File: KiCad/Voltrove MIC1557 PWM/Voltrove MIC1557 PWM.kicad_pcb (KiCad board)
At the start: 2 copper layers, 70 x 20 mm, 32 parts, among them IC1 DS1809Z-010+, IC2 NCV4264-2ST50T3G, J1 BAT-, J2 510-, J3 VIN+, J4 PAD_Fire2, J5 PAD_Fire1, J6 VM-, J7 VM+, Q1 SSM3J334R_LF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

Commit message: v2
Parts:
- moved J7 1.66 mm to (128.0, 105.0)
- moved J6 1.50 mm to (125.0, 105.0)
- moved R4 1.00 mm to (175.4, 107.4)
- moved R1 0.50 mm to (168.4, 107.4)
- moved R3 0.50 mm to (173.1, 107.4)
- turned Q1 to 270 degrees
- turned R5 to 0 degrees
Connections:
- net Net-(C3-Pad1) renamed /5V+toC3
- net Net-(C4-Pad1) renamed /D2toSTR
- net Net-(D1-Pad1) renamed /POT0%
- net Net-(D1-Pad3) renamed /POT100%
- net Net-(D3-Pad1) renamed /VIN+toFire1
- net Net-(D3-Pad2) renamed /R5toD3
- net Net-(IC1-Pad6) renamed /POTWIPER
- net Net-(R2-Pad2) renamed /U1toR2
- net Net-(R3-Pad1) renamed /U1OUT
- net Net-(R5-Pad2) renamed /VIN+toR5
- C2 pad 1: /VIN+ -> /VIN+fromQ1Source
- IC2 pad 1: /VIN+ -> /VIN+fromQ1Source
- J3 pad 1: /VIN+ -> /VIN+toSwitch
- J4 pad 1: /VIN+ -> /VIN+toQ1Drain
- J7 pad 1: /VIN+ -> /VIN+fromQ1Source
- Q1 pad 2: /VIN+ -> /VIN+fromQ1Source
- Q1 pad 3: /VIN+ -> /VIN+toQ1Drain
- R2 pad 1: /VIN+ -> /VIN+fromQ1Source
- S1 pad 3: /VIN+ -> /VIN+toQ1Drain
- S1 pad 4: /VIN+ -> /VIN+toQ1Drain
- S4 pad 1: /VIN+ -> /VIN+toSwitch
- U1 pad 4: /VIN+ -> /VIN+fromQ1Source
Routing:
- net /VIN+: track 160.5 -> 0.00 mm, vias 2 -> 0
- net /VIN+fromQ1Source: track 0.00 -> 97.0 mm, vias 0 -> 3
- net /VIN+toQ1Drain: track 0.00 -> 86.1 mm, vias 0 -> 1
- net /POTWIPER: track 22.9 -> 39.9 mm
- net /5V+toC3: track 42.8 -> 30.6 mm, vias 2 -> 3
- net Net-(C1-Pad1): track 37.8 -> 25.8 mm
- net /VIN+toFire1: track 74.8 -> 84.5 mm, vias 1 -> 0
- net Net-(Q2-Pad4): track 33.7 -> 27.4 mm
- net /VIN+toSwitch: track 0.00 -> 5.62 mm
- net GND: track 135.5 -> 129.9 mm, vias 3 -> 1
- net /VIN+toR5: track 9.18 -> 5.73 mm
- net /UP: track 18.2 -> 20.7 mm
- net /D2toSTR: track 35.3 -> 37.7 mm
- net /R5toD3: track 5.01 -> 3.72 mm

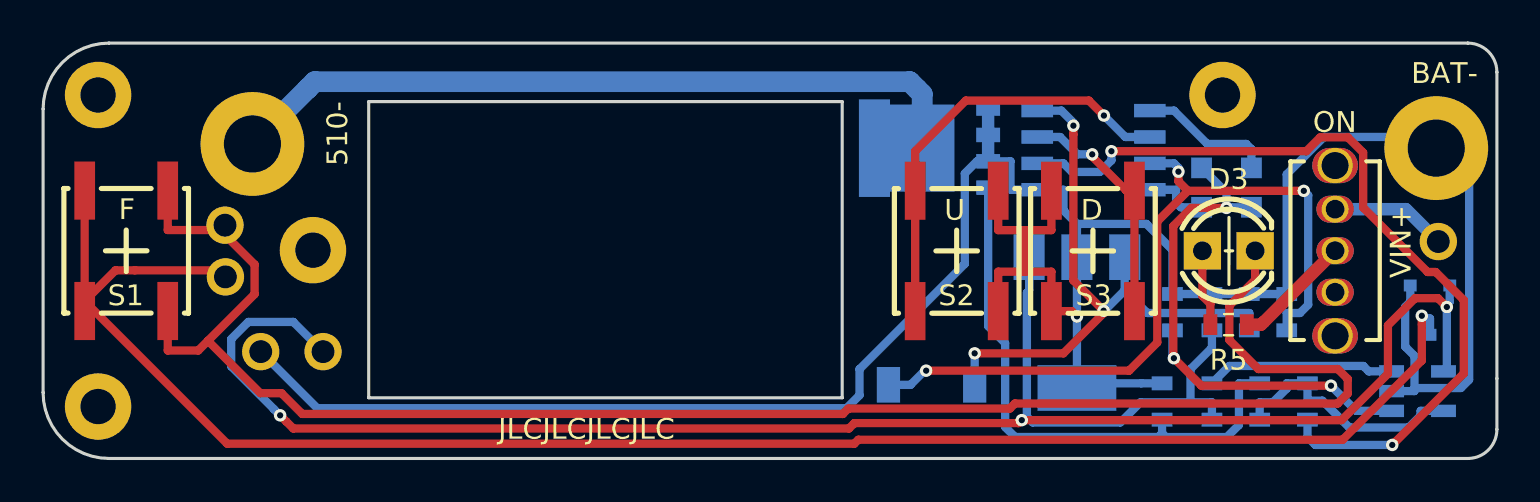
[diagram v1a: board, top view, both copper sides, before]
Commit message: v3 suggestions from David
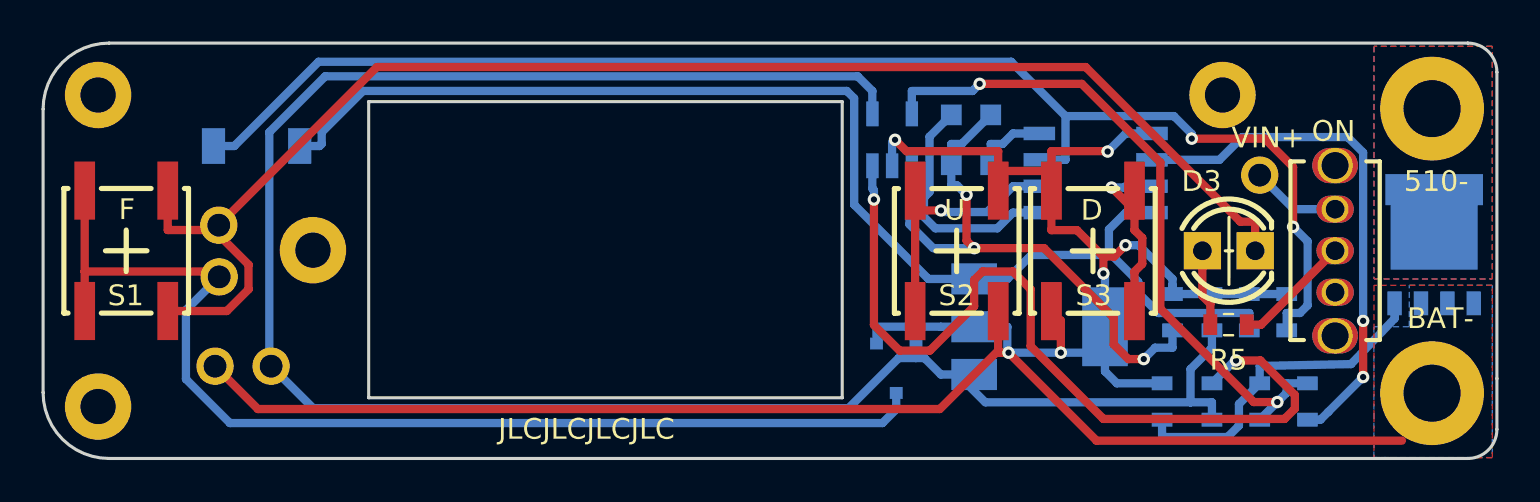
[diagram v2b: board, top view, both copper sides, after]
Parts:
- PAD4_VM: value Mount_PAD -> Mount_PAD_VM; footprint ATI DNA-C PCB:Mount_PAD -> Voltrove MIC1557 PWM:Mount_PAD_VM
- moved J2 56.8 mm to (181.4, 93.3)
- moved D2 34.5 mm to (124.8, 95.1)
- moved U1 28.0 mm to (155.4, 94.8), turned to 90 degrees
- moved Q2 26.5 mm to (181.5, 97.8), turned to 180 degrees
- moved Q1 25.9 mm to (155.6, 105.8)
- moved D1 12.5 mm to (159.2, 94.8), turned to 180 degrees
- moved J1 11.8 mm to (181.4, 107.0)
- moved J3 9.18 mm to (173.1, 96.5)
- moved J7 2.60 mm to (125.5, 105.7)
- moved J6 2.31 mm to (122.8, 105.7)
- moved IC2 1.81 mm to (162.5, 103.8), turned to 90 degrees
- moved IC1 1.10 mm to (165.2, 96.4), turned to 0 degrees
- moved J4 0.30 mm to (123.0, 101.4)
- moved J5 0.30 mm to (123.0, 98.9)
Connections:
- net /VIN+fromQ1Source renamed /VIN+VM+
- Q2 pad 6: (no net) -> /510-
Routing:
- net /510-: track 36.3 -> 0.00 mm
- net /U1toR2: track 9.10 -> 41.3 mm, vias 0 -> 2
- net /VIN+toQ1Drain: track 86.1 -> 54.1 mm, vias 1 -> 0
- net /D2toSTR: track 37.7 -> 68.2 mm, vias 3 -> 2
- net /5V+toC3: track 30.6 -> 60.3 mm, vias 3 -> 0
- net /U1OUT: track 12.0 -> 32.6 mm, vias 0 -> 2
- net /POTWIPER: track 39.9 -> 25.3 mm
- net /VIN+toFire1: track 84.5 -> 69.9 mm
- net Net-(Q2-Pad4): track 27.4 -> 16.7 mm
- net GND: track 129.9 -> 120.5 mm, vias 1 -> 6
- net /UP: track 20.7 -> 12.3 mm
- net /POT100%: track 6.56 -> 11.6 mm
- net Net-(C1-Pad1): track 25.8 -> 28.2 mm
- net /Down: track 11.6 -> 9.64 mm
- net /VIN+toSwitch: track 5.62 -> 4.31 mm
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- added copper zone on B.Cu, net /510-
- added copper zone on F.Cu, net /510-
- added copper zone on B.Cu, net GND
- added copper zone on F.Cu, net GND
